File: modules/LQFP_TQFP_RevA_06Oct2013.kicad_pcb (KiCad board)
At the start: 2 copper layers, 5 parts

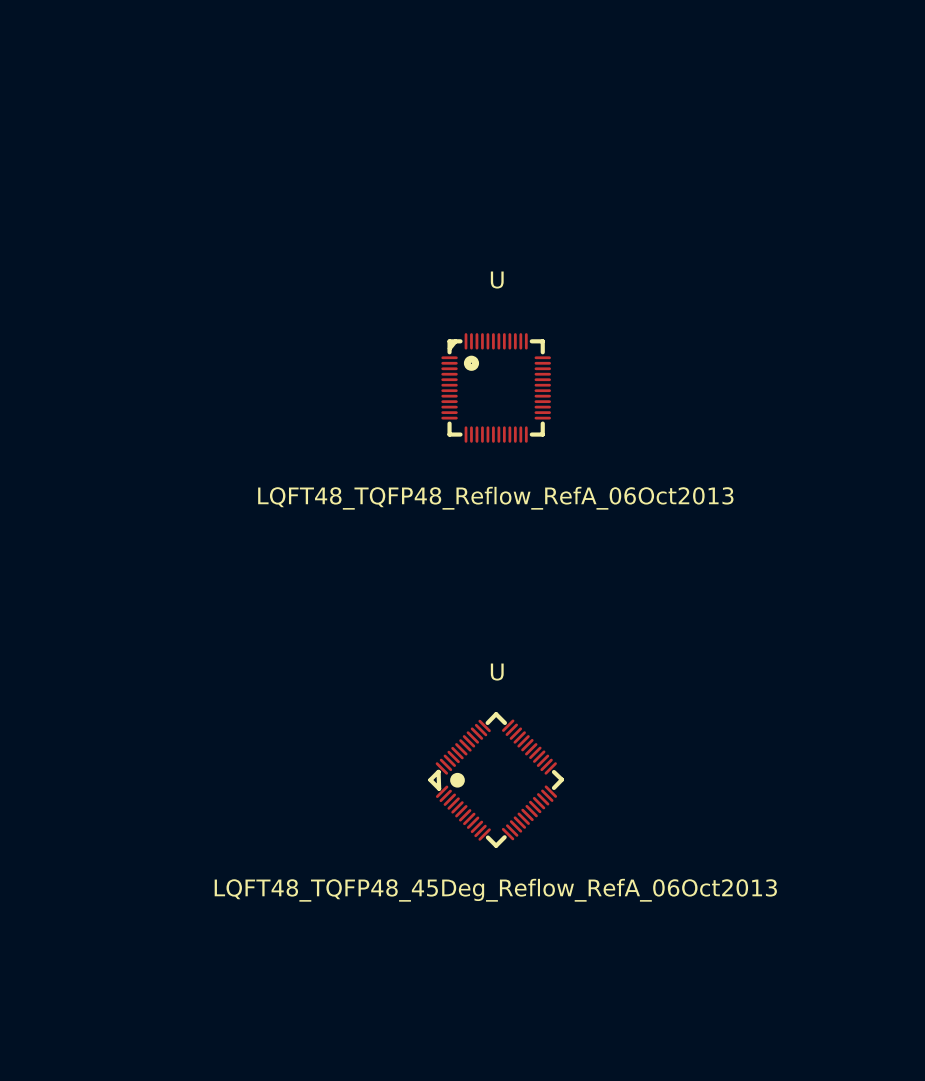
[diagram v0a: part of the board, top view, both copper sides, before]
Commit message: LQFP48/TQFP48 update. Symbols for LEM hall effect current transducer added.
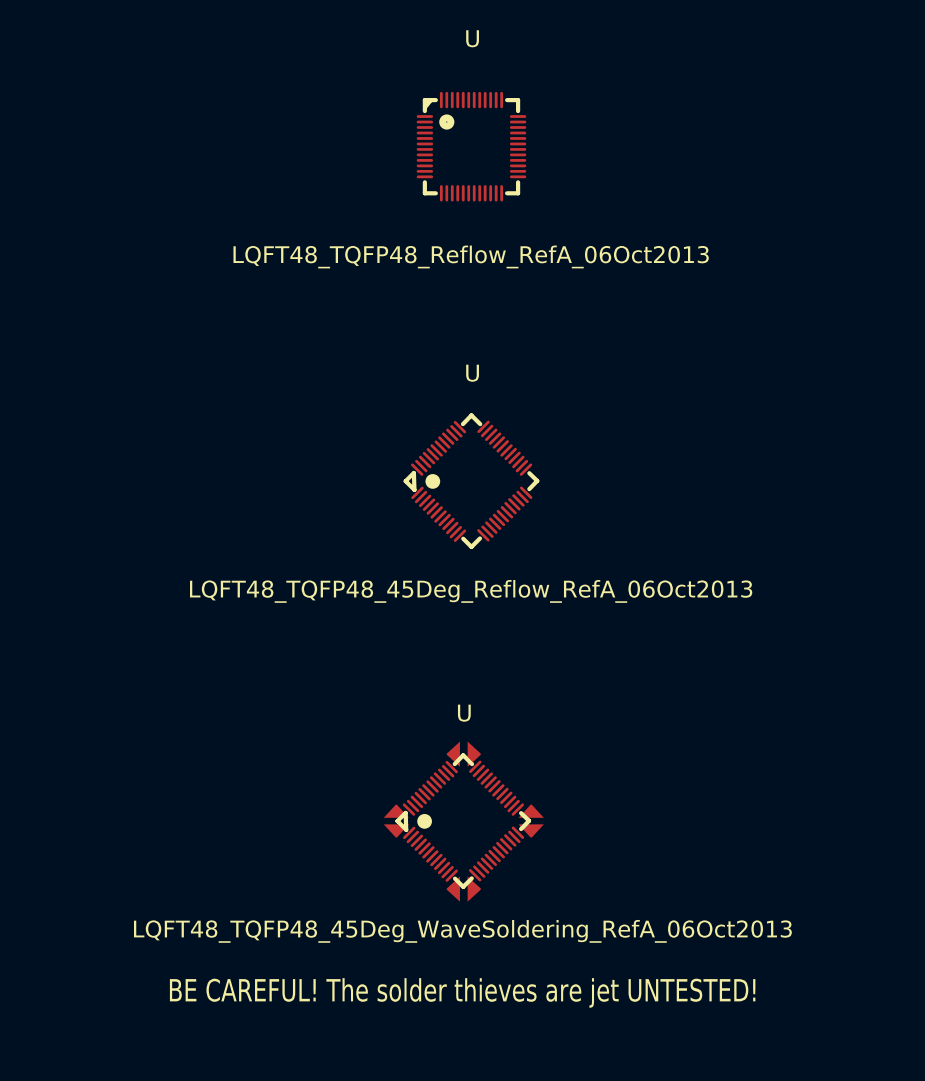
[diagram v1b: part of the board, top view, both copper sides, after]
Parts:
- added U: LQFT48_TQFP48_45Deg_WaveSoldering_RefA_06Oct2013, LQFT48_TQFP48_45Deg_WaveSoldering_RefA_06Oct2013, F.Cu at (185.2, 111.2)
- moved U 27.3 mm to (186.0, 80.2)
- moved U 22.1 mm to (186.0, 49.8)
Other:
- board text added: "BE CAREFUL! The solder thieves are jet UNTESTED!"

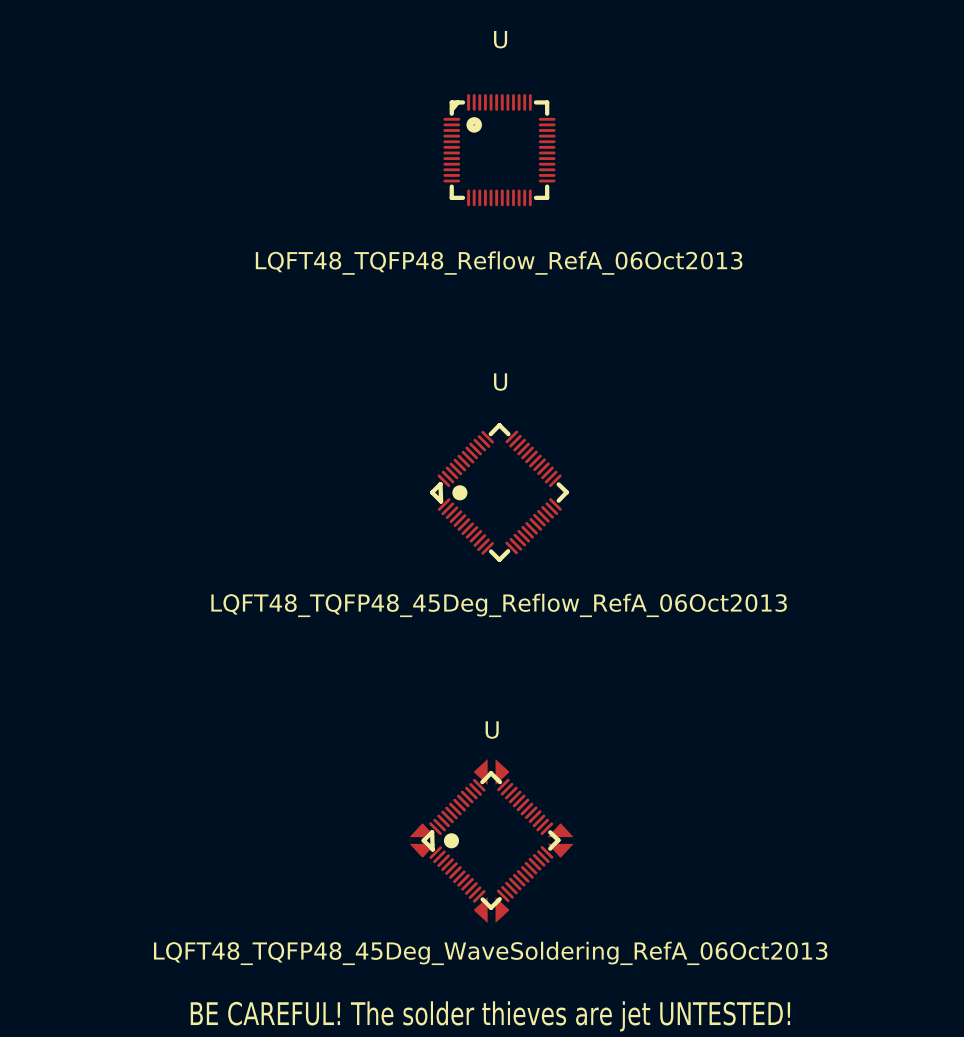
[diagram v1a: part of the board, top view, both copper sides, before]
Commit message: Footprind and 3d modell of LEM HTFS-series hall effect current transducers added.
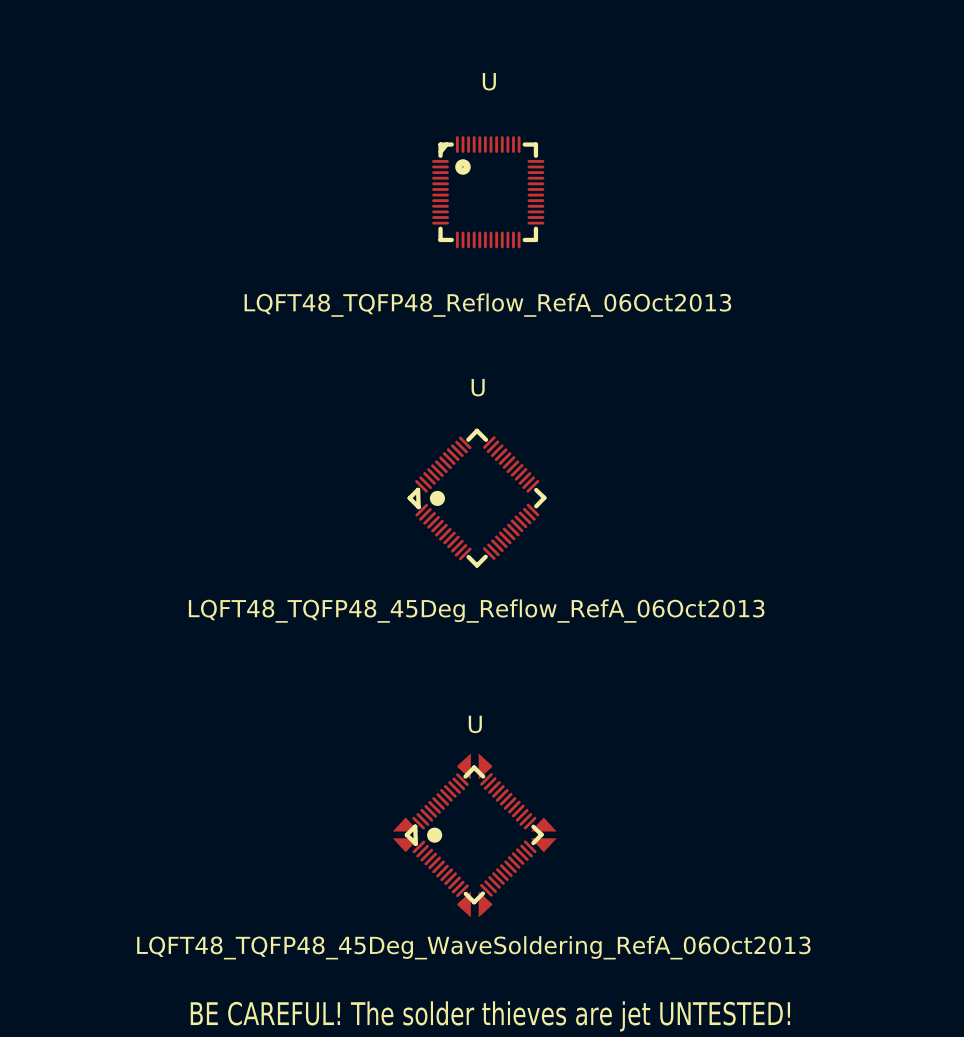
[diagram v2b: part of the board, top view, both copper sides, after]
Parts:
- moved U 3.88 mm to (185.0, 53.5)
- moved U 2.06 mm to (184.0, 80.8)
- moved U 1.58 mm to (183.8, 110.8)
